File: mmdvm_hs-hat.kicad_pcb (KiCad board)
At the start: 2 copper layers, 65.1 x 30.2 mm, 138 parts, among them P1 BOOT0, P2 DISPLAY, P3 SMA, P4 STLINK, SW1 SW_DIP_x01, U1 ADF7021, U2 STM32F103C8T6, X1 TCXO, Y1 8MHz

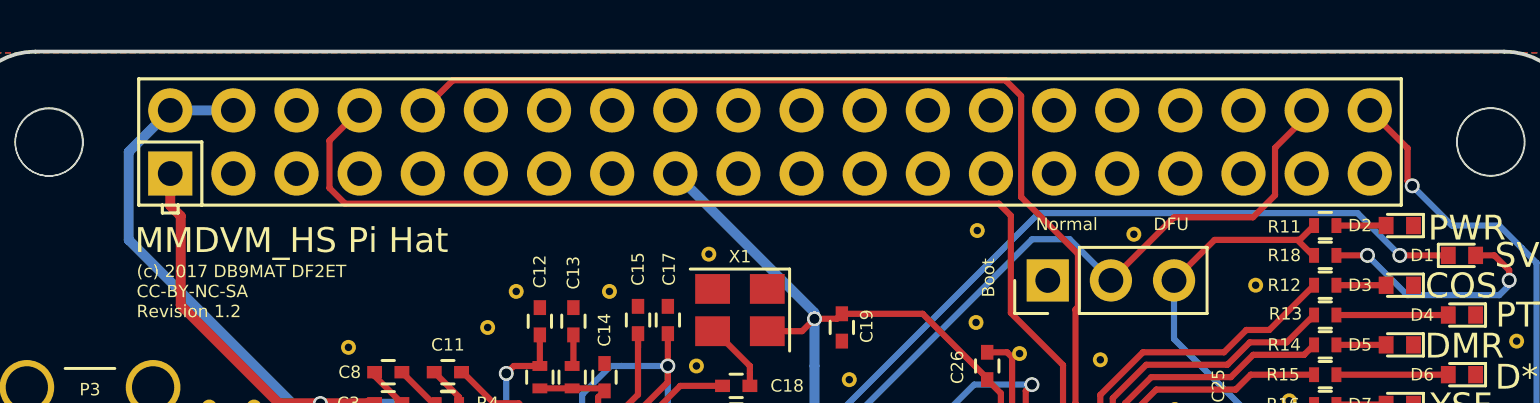
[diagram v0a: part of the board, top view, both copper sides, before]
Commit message: Small changes with package for this board rev (needed to modelize the enclosure).
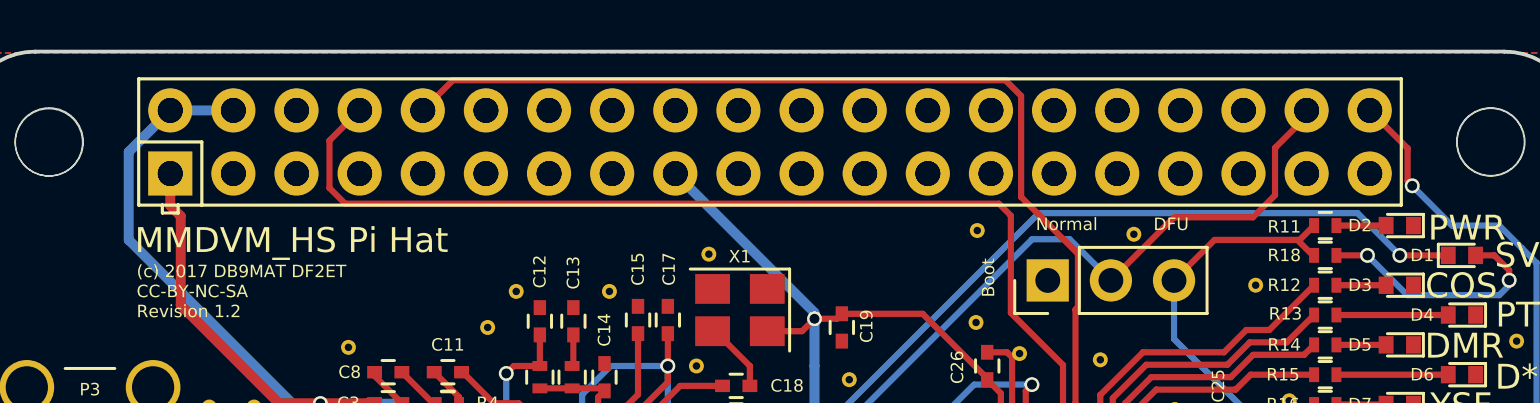
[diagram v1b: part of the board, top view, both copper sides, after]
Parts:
- added REF**: PinSocket_2x20_P2.54mm_Vertical, Connector_PinSocket_2.54mm:PinSocket_2x20_P2.54mm_Vertical, B.Cu at (163.8, 110.5)
